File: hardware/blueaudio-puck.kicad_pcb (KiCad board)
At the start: 2 copper layers, 60 x 55 mm, 45 parts, among them J1 USB-C, J2 3.5mm, J3 OLED, J4 BATT, J5 PROG, SW1 MODE, SW2 RESET, U1 ESP32-WROOM-32U, U2 PCM5102A, U3 MCP73831-2-OT, U4 AP2112K-3.3, U5 LP2985-3.3

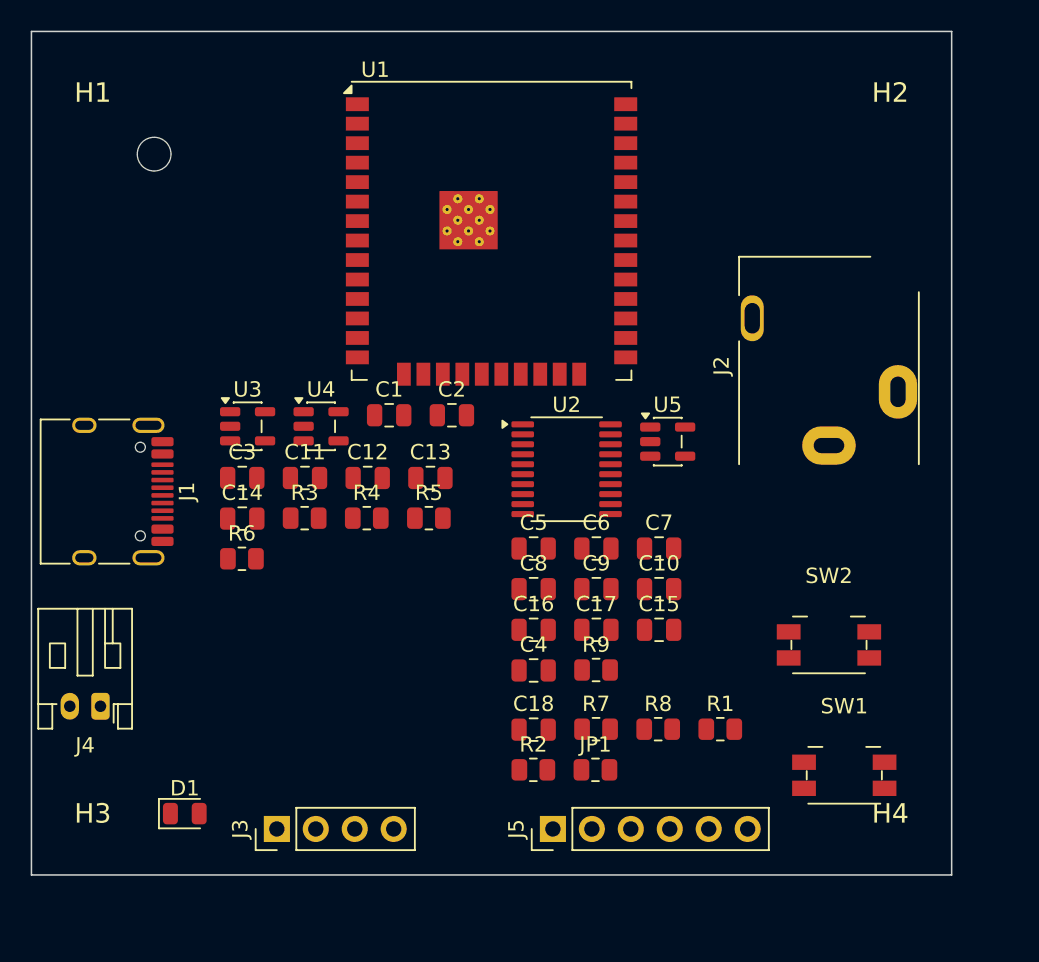
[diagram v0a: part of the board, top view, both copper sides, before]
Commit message: Enhance BlueAudio Puck design with auto-reset functionality and routing improvements
- Updated `blueaudio-puck.kicad_pro` to include top-level schematic sheet.
- Enhanced `design.py` with detailed documentation on auto-reset behavior and added components for manual reset.
- Modified net connections to reflect changes in auto-reset circuitry.
- Improved PCB generation script (`gen_pcb.py`) to handle new component placements and added ground pours for better GND connectivity.
- Introduced a new routing script (`route.py`) for efficient signal routing, ensuring no nets are left half-connected.
- Implemented a grid-based routing algorithm that prioritizes clear paths and avoids conflicts with existing components.
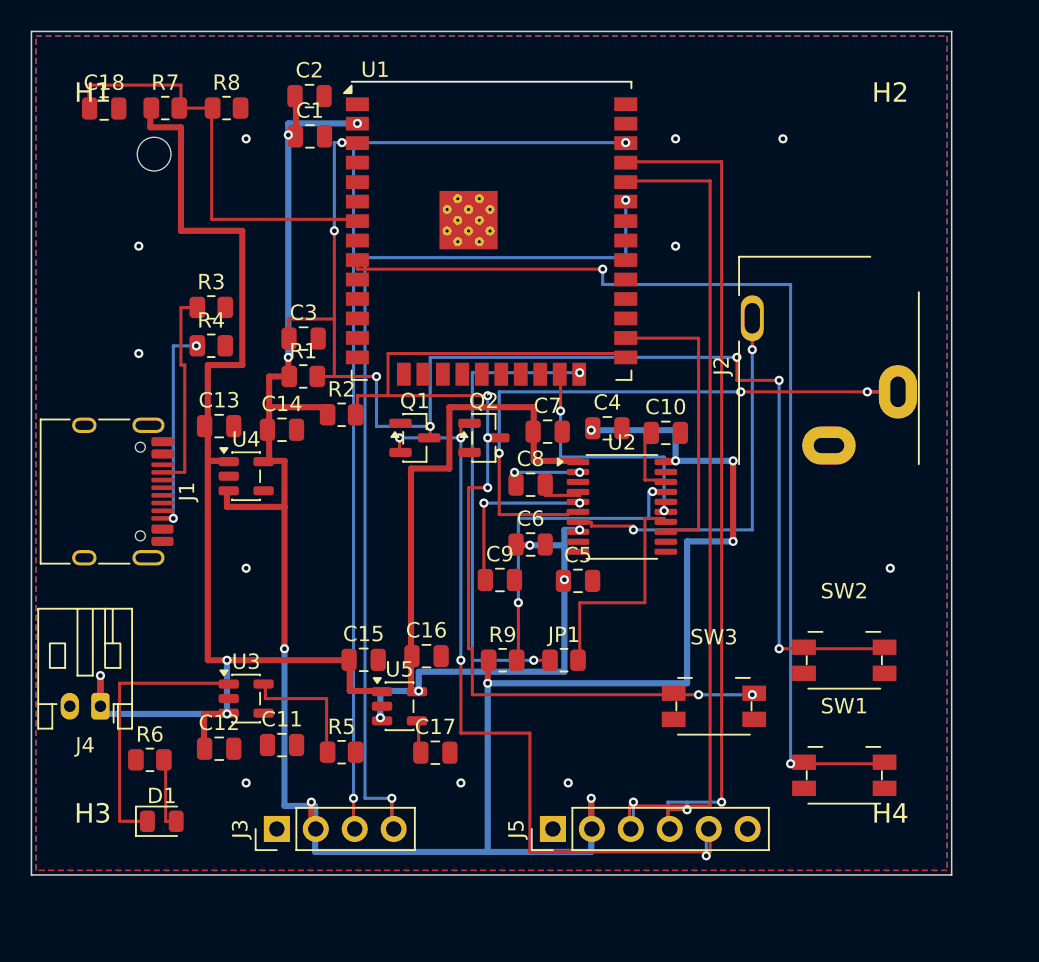
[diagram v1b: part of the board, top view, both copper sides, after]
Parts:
- added Q1: MMBT3904, SOT-23, F.Cu at (25.0, 26.5)
- added Q2: MMBT3904, SOT-23, F.Cu at (29.5, 26.5)
- added SW3: BOOT, Panasonic_EVQPUJ_EVQPUA, F.Cu at (44.5, 44.0)
- moved R8 49.3 mm to (12.7, 5.00)
- moved R7 49.3 mm to (8.72, 5.00)
- moved C18 49.2 mm to (4.75, 5.03)
- moved R1 35.6 mm to (17.7, 22.5)
- moved R2 26.3 mm to (20.2, 25.0)
- moved U5 24.6 mm to (24.0, 44.0)
- moved C2 22.8 mm to (18.1, 4.21)
- moved C12 20.1 mm to (12.2, 46.8)
- moved C15 19.4 mm to (21.7, 41.0)
- moved C1 18.9 mm to (18.2, 6.84)
- moved U3 17.8 mm to (14.0, 43.5)
- moved C11 17.5 mm to (16.3, 46.5)
- moved C4 16.5 mm to (37.6, 25.9)
- moved R5 16.3 mm to (20.2, 47.0)
- moved R4 15.1 mm to (11.7, 20.5)
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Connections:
- J5 pad 1: +3V3 -> GND
- J5 pad 2: GND -> +3V3
- J5 pad 3: EN -> RXD0
- J5 pad 4: IO0 -> TXD0
- J5 pad 5: TXD0 -> DTR
- J5 pad 6: RXD0 -> RTS
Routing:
- net +3V3: track 0.00 -> 149.2 mm, vias 0 -> 11
- net EN: track 0.00 -> 85.2 mm, vias 0 -> 7
- net VBAT: track 0.00 -> 79.0 mm, vias 0 -> 3
- net IO0: track 0.00 -> 68.2 mm, vias 0 -> 5
- net BTN_MODE: track 0.00 -> 67.0 mm, vias 0 -> 2
- net I2C_SCL: track 0.00 -> 64.5 mm, vias 0 -> 2
- net +3V3A: track 0.00 -> 62.2 mm, vias 0 -> 5
- net I2C_SDA: track 0.00 -> 61.8 mm, vias 0 -> 2
- net TXD0: track 0.00 -> 56.2 mm, vias 0 -> 2
- net RXD0: track 0.00 -> 55.2 mm, vias 0 -> 1
- net DTR: track 0.00 -> 53.5 mm, vias 0 -> 4
- net AUDIO_L: track 0.00 -> 41.5 mm, vias 0 -> 3
- net I2S_DATA_MCU: track 0.00 -> 30.8 mm, vias 0 -> 2
- net VBAT_SENSE: track 0.00 -> 27.8 mm
- net AUDIO_R: track 0.00 -> 27.5 mm, vias 0 -> 2
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- added copper zone on B.Cu, net GND
- added copper zone on F.Cu, net GND
